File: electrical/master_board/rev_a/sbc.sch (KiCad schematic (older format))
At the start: 21 parts, among them CN94 RASPI;F2X20, SW2 PUSH_BUTTON;6x6x9.5H, U2 MCP7940;SOIC8, U3 CAT24C32;SOIC8, X1 32.768kHZ;3.2x1.5MM

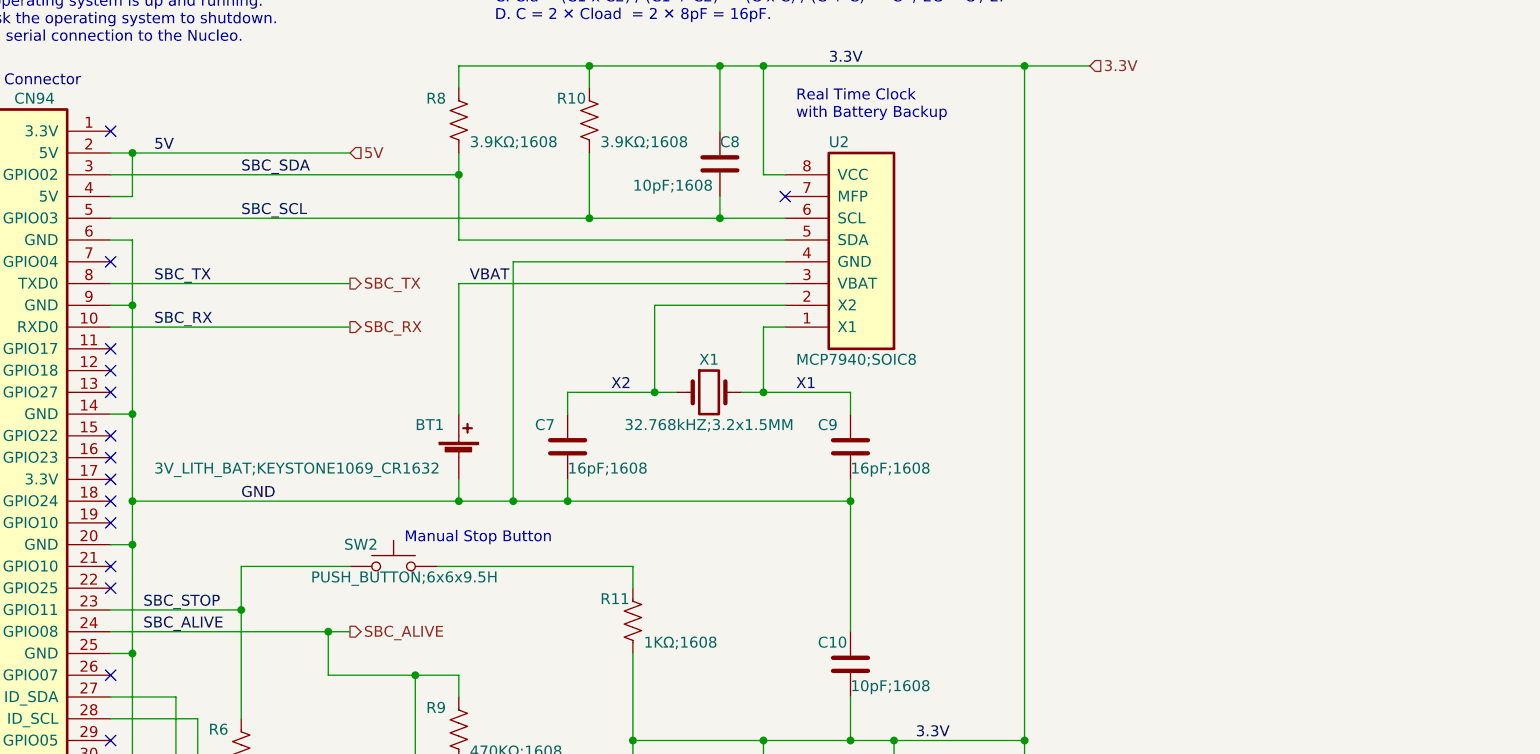
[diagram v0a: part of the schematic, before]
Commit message: Changing footprints and moving things around on the PCB.
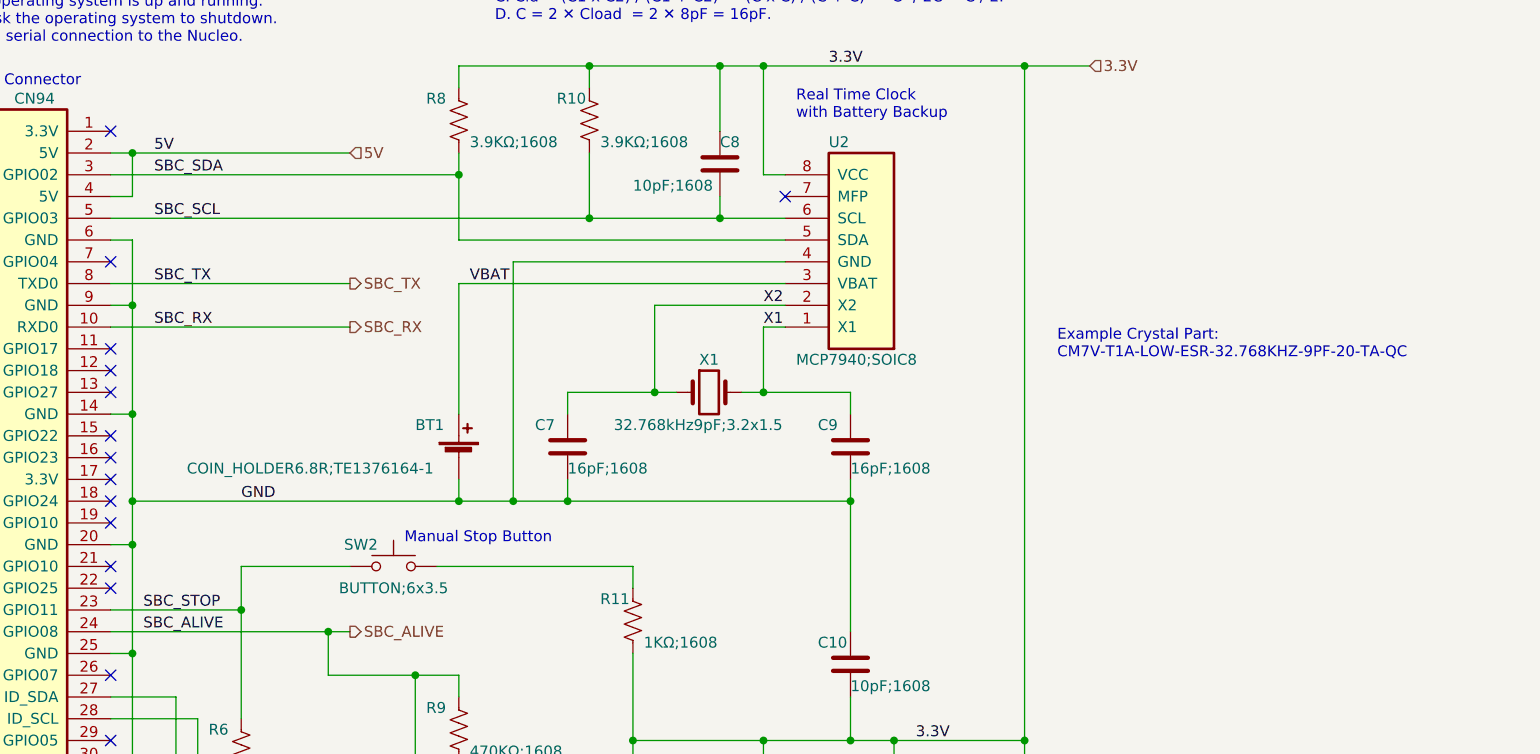
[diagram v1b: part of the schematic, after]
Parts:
- BT1: value 3V_LITH_BAT;KEYSTONE1069_CR1632 -> COIN_HOLDER6.8R;TE1376164-1; footprint HR2:KEYSTONE_1069_1x10MM_CR1632 -> HR2:TE1376164-1_COINHOLDER6.8
- SW2: value PUSH_BUTTON;6x6x9.5H -> BUTTON;6x3.5; footprint Button_Switch_SMD:SW_SPST_PTS645 -> HR2:BUTTON_6x3.5
- X1: value 32.768kHZ;3.2x1.5MM -> 32.768kHz9pF;3.2x1.5; footprint Crystal:Crystal_SMD_3225-4Pin_3.2x2.5mm_HandSoldering -> Crystal:Crystal_SMD_5032-2Pin_5.0x3.2mm
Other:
- note added: "Example Crystal Part:\nCM7V-T1A-LOW-ESR-32.768KHZ-9PF-20-TA-QC"
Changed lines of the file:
@@
 AR Path="/5FA587FE/5F4F5A10" Ref="X?"  Part="1"
 F 0 "X1" H 6650 3350 50  0000 C CNN
-F 1 "32.768kHZ;3.2x1.5MM" H 6650 3050 50  0000 C CNN
-F 2 "Crystal:Crystal_SMD_3225-4Pin_3.2x2.5mm_HandSoldering" H 6650 3200 50  0001 C CNN
+F 1 "32.768kHz9pF;3.2x1.5" H 6600 3050 50  0000 C CNN
+F 2 "Crystal:Crystal_SMD_5032-2Pin_5.0x3.2mm" H 6650 3200 50  0001 C CNN
 F 3 "~" H 6650 3200 50  0001 C CNN
 	1    6650 3200
@@
 AR Path="/5FA587FE/5F4E022E" Ref="BT?"  Part="1"
 F 0 "BT1" H 5300 3650 50  0000 L CNN
-F 1 "3V_LITH_BAT;KEYSTONE1069_CR1632" H 4100 3450 50  0000 L CNN
-F 2 "HR2:KEYSTONE_1069_1x10MM_CR1632" V 5500 3560 50  0001 C CNN
+F 1 "COIN_HOLDER6.8R;TE1376164-1" H 4250 3450 50  0000 L CNN
+F 2 "HR2:TE1376164-1_COINHOLDER6.8" V 5500 3560 50  0001 C CNN
 F 3 "~" V 5500 3560 50  0001 C CNN
 	1    5500 3500
@@
 Wire Wire Line
 	5500 2200 5500 2100
-Text Label 4500 2400 0    50   ~ 0
+Text Label 4100 2400 0    50   ~ 0
 SBC_SCL
-Text Label 4500 2200 0    50   ~ 0
+Text Label 4100 2200 0    50   ~ 0
 SBC_SDA
 Text Label 5550 2700 0    50   ~ 0
 VBAT
-Text Label 6200 3200 0    50   ~ 0
+Text Label 6900 2800 0    50   ~ 0
 X2
-Text Label 7050 3200 0    50   ~ 0
+Text Label 6900 2900 0    50   ~ 0
 X1
 Wire Wire Line
@@
 AR Path="/5F4877FA/5F8FBAFA" Ref="SW2"  Part="1"
 F 0 "SW2" H 5050 4100 50  0000 C CNN
-F 1 "PUSH_BUTTON;6x6x9.5H" H 5250 3950 50  0000 C CNN
-F 2 "Button_Switch_SMD:SW_SPST_PTS645" H 5200 4200 50  0001 C CNN
+F 1 "BUTTON;6x3.5" H 5200 3900 50  0000 C CNN
+F 2 "HR2:BUTTON_6x3.5" H 5200 4200 50  0001 C CNN
 F 3 "~" H 5200 4200 50  0001 C CNN
 	1    5200 4000
@@
 	7300 4300 7300 3700
 Connection ~ 7300 3700
+Text Notes 8250 3050 0    50   ~ 0
+Example Crystal Part:\nCM7V-T1A-LOW-ESR-32.768KHZ-9PF-20-TA-QC
 $EndSCHEMATC

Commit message: Lots of work on the PCB.
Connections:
- net WP: now reaches JP1.1, R14.2, U3.7 (WP)
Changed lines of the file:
@@
 Text Notes 8250 3050 0    50   ~ 0
 Example Crystal Part:\nCM7V-T1A-LOW-ESR-32.768KHZ-9PF-20-TA-QC
+Text Label 7750 5400 0    50   ~ 0
+WP
 $EndSCHEMATC

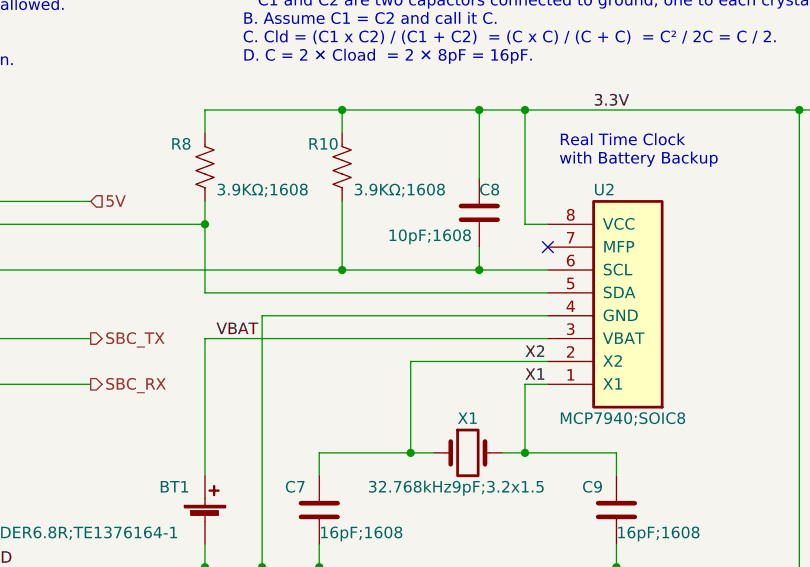
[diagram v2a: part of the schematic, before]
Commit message: Weaving traces from NE corner around the heat sink holes.
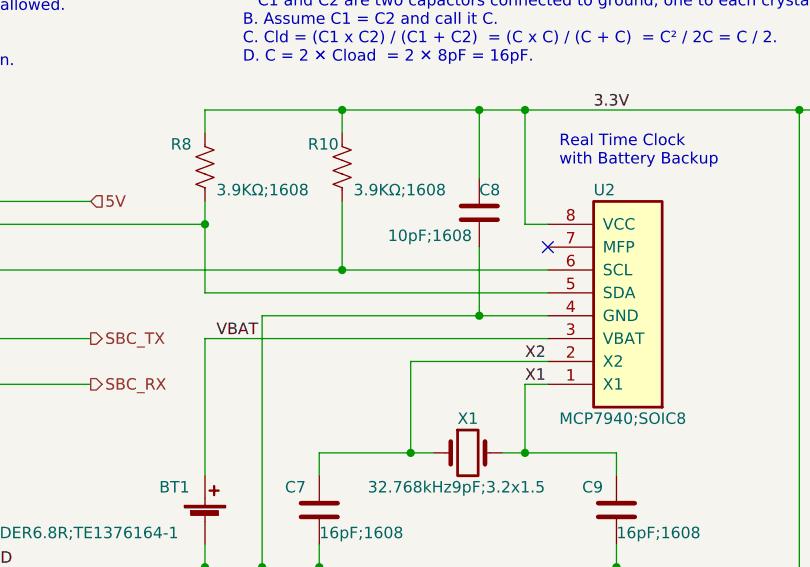
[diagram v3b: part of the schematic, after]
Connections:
- net GND: now also C8.2
- net SBC_SCL: no longer C8.2
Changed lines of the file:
@@
 	6900 2200 6900 1700
-Wire Wire Line
-	6900 1700 6700 1700
 Wire Wire Line
 	6100 1700 6100 1800
@@
 	4200 5600 6300 5600
 Wire Wire Line
-	8100 4800 8100 1700
-Wire Wire Line
 	8100 1700 6900 1700
 Connection ~ 8100 4800
@@
 	5500 3700 4000 3700
 Wire Wire Line
-	5750 2600 7000 2600
+	5750 2600 6700 2600
 Wire Wire Line
 	5750 3700 5500 3700
@@
 	5500 5400 5500 5800
 $Comp
+L Device:C C10
+U 1 1 5FA44A8F
+P 7300 4450
+AR Path="/5F4877FA/5FA44A8F" Ref="C10"  Part="1"
+AR Path="/5FA587FE/5FA44A8F" Ref="C?"  Part="1"
+F 0 "C10" H 7150 4550 50  0000 L CNN
+F 1 "10pF;1608" H 7300 4350 50  0000 L CNN
+F 2 "Capacitor_SMD:C_0603_1608Metric" H 7338 4300 50  0001 C CNN
+F 3 "~" H 7300 4450 50  0001 C CNN
+	1    7300 4450
+	1    0    0    -1
+$EndComp
+Wire Wire Line
+	7300 4600 7300 4800
+Connection ~ 7300 4800
+Wire Wire Line
+	7300 4800 6900 4800
+Wire Wire Line
+	7300 4300 7300 3700
+Connection ~ 7300 3700
+Text Notes 8250 3050 0    50   ~ 0
+Example Crystal Part:\nCM7V-T1A-LOW-ESR-32.768KHZ-9PF-20-TA-QC
+Text Label 7750 5400 0    50   ~ 0
+WP
+Wire Wire Line
+	6700 1700 6100 1700
+Wire Wire Line
+	6900 1700 6700 1700
+Connection ~ 6700 1700
+Wire Wire Line
+	6700 2000 6700 1700
+Wire Wire Line
+	8100 4800 8100 1700
+$Comp
 L Device:C C8
 U 1 1 5FA24EA3
@@
 $EndComp
 Wire Wire Line
-	6700 2300 6700 2400
-Wire Wire Line
-	6100 2400 6700 2400
-Connection ~ 6700 2400
-Wire Wire Line
-	6700 2400 7000 2400
-Wire Wire Line
-	6700 2000 6700 1700
-Connection ~ 6700 1700
-Wire Wire Line
-	6700 1700 6100 1700
-$Comp
-L Device:C C10
-U 1 1 5FA44A8F
-P 7300 4450
-AR Path="/5F4877FA/5FA44A8F" Ref="C10"  Part="1"
-AR Path="/5FA587FE/5FA44A8F" Ref="C?"  Part="1"
-F 0 "C10" H 7150 4550 50  0000 L CNN
-F 1 "10pF;1608" H 7300 4350 50  0000 L CNN
-F 2 "Capacitor_SMD:C_0603_1608Metric" H 7338 4300 50  0001 C CNN
-F 3 "~" H 7300 4450 50  0001 C CNN
-	1    7300 4450
-	1    0    0    -1
-$EndComp
-Wire Wire Line
-	7300 4600 7300 4800
-Connection ~ 7300 4800
-Wire Wire Line
-	7300 4800 6900 4800
-Wire Wire Line
-	7300 4300 7300 3700
-Connection ~ 7300 3700
-Text Notes 8250 3050 0    50   ~ 0
-Example Crystal Part:\nCM7V-T1A-LOW-ESR-32.768KHZ-9PF-20-TA-QC
-Text Label 7750 5400 0    50   ~ 0
-WP
+	6100 2400 7000 2400
+Wire Wire Line
+	6700 2300 6700 2600
+Connection ~ 6700 2600
+Wire Wire Line
+	6700 2600 7000 2600
 $EndSCHEMATC
